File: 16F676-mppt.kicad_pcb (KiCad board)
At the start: 2 copper layers, 96.5 x 87.6 mm, 54 parts, among them J1 S+, J2 S-, J3 VB+, J4 VB-, Q1 BUK9511-55A127, Q2 BUK9511-55A127, Q3 2N2222A, Q4 2N2222A, Q5 2N2907A, Q6 2N2222A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

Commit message: Fix Bootstrap problem.
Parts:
- C2: value 10uF 50v -> 4.7uF 50v
- R1: value 2.2k -> 10k
- R15: value 2.2k -> 3.3k
- R2, R4: value 100k -> 47k
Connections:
- C2 pad 1: Net-(C2-Pad1) -> /BootStrap
- C3 pad 1: /BootStrap -> Net-(C3-Pad1)
- C4 pad 1: /BootStrap -> Net-(C3-Pad1)
- D3 pad 1: Net-(C2-Pad1) -> /BootStrap
- D3 pad 2: /BootStrap -> Net-(C7-Pad1)
- Q4 pad 3: Net-(C2-Pad1) -> /BootStrap
- R11 pad 1: /BootStrap -> Net-(C3-Pad1)
- R14 pad 1: /BootStrap -> Net-(C3-Pad1)
- R16 pad 2: /BootStrap -> Net-(C3-Pad1)
- R9 pad 1: Net-(C2-Pad1) -> /BootStrap
- U1 pad 3: /BootStrap -> Net-(C3-Pad1)
- U2 pad 8: /BootStrap -> Net-(C3-Pad1)
- U3 pad 1: /BootStrap -> Net-(C3-Pad1)
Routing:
- net Net-(C3-Pad1): track 0.00 -> 101.4 mm
- net /BootStrap: track 113.1 -> 44.7 mm
- net Net-(C2-Pad1): track 44.7 -> 0.00 mm
- net Net-(C7-Pad1): track 67.4 -> 81.8 mm

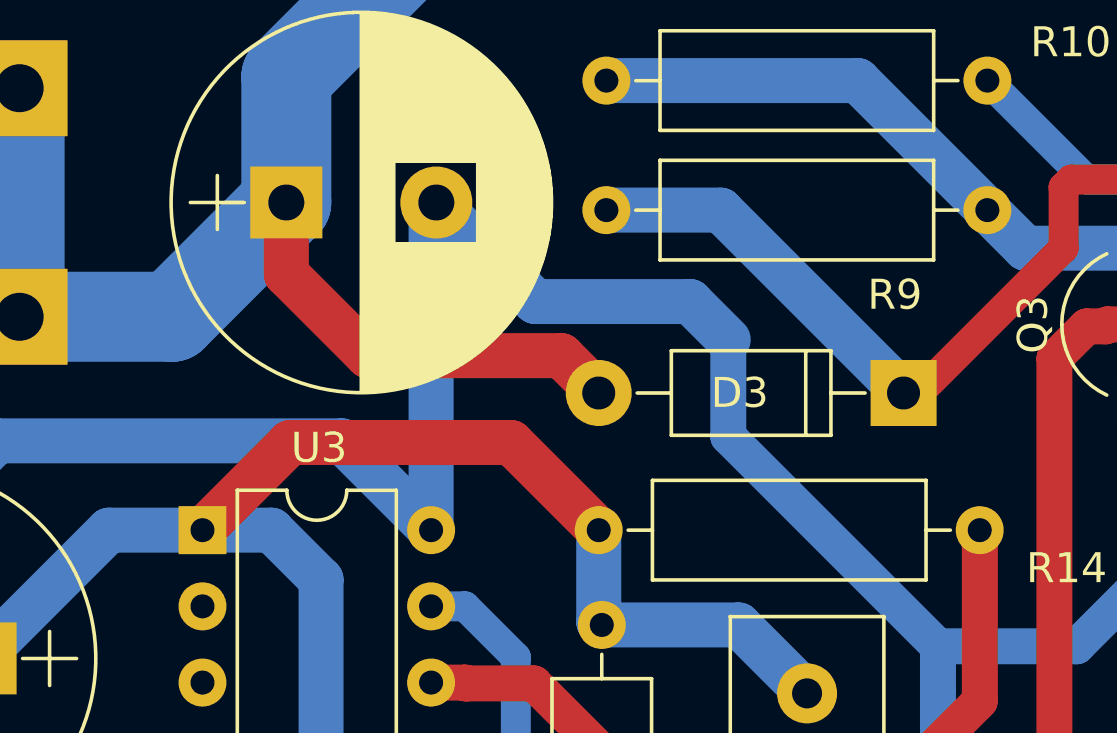
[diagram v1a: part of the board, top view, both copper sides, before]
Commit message: Revert and change diode.
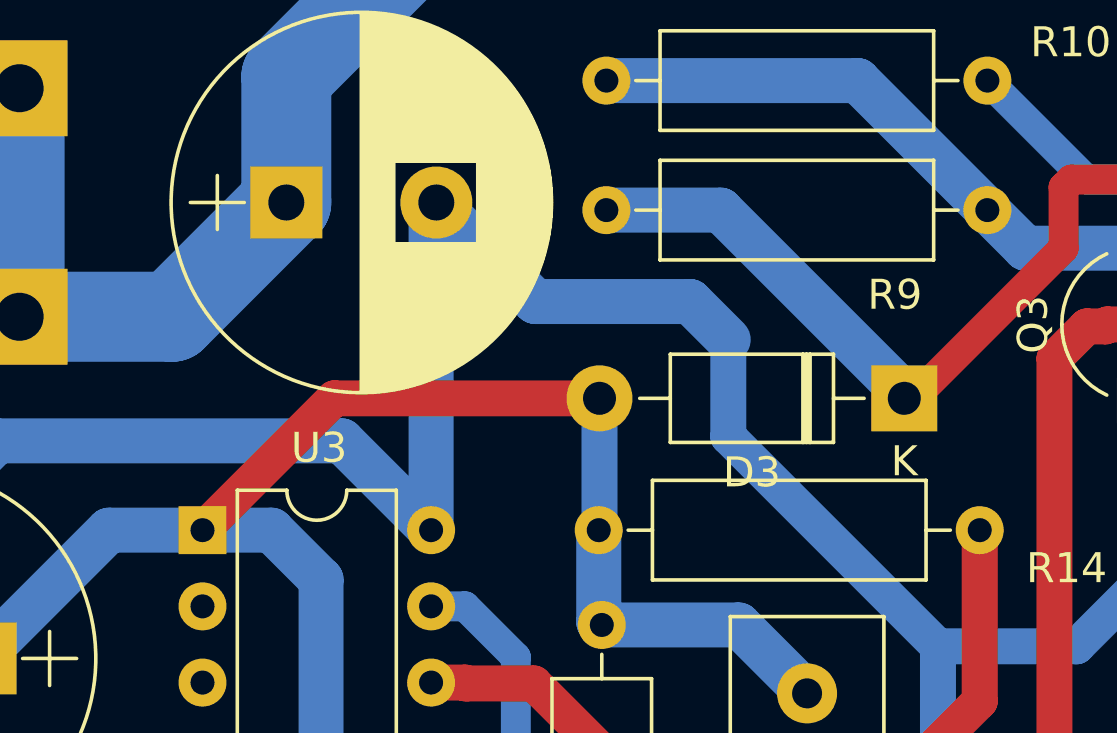
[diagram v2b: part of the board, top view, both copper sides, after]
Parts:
- D3: value 1N4148 -> 1N5819; footprint Diodes_THT:D_DO-41_SOD81_P10.16mm_Horizontal -> Diode_THT:D_DO-41_SOD81_P10.16mm_Horizontal
- moved D3 0.18 mm to (68.4, 28.9)
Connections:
- D3 pad 2: Net-(C7-Pad1) -> Net-(C3-Pad1)
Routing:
- net Net-(C7-Pad1): track 81.8 -> 67.4 mm
- net Net-(C3-Pad1): track 101.4 -> 105.2 mm

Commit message: Update SCH and PCB files.
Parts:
- added C6: 22p, Capacitor_THT:C_Rect_L4.6mm_W2.0mm_P2.50mm_MKS02_FKP02, F.Cu at (36.0, 35.8)
- added C8: 22p, Capacitor_THT:C_Rect_L4.6mm_W2.0mm_P2.50mm_MKS02_FKP02, F.Cu at (36.0, 39.0)
- added D12: BZX79C12, Diode_THT:D_DO-35_SOD27_P2.54mm_Vertical_AnodeUp, F.Cu at (95.9, 18.5)
- added Y1: 12MHz, Crystal:Crystal_HC49-U_Vertical, F.Cu at (40.5, 39.9)
- C2, C3, C5: footprint Capacitors_THT:CP_Radial_D12.5mm_P5.00mm -> Capacitor_THT:CP_Radial_D8.0mm_P2.50mm
- D3: value 1N5819 -> 1N4148; footprint Diode_THT:D_DO-41_SOD81_P10.16mm_Horizontal -> Diode_THT:D_DO-35_SOD27_P7.62mm_Horizontal
- R1: value 10k -> 1k
- R2, R4: value 47k -> 100k
- moved R11 18.6 mm to (70.8, 50.2), turned to 180 degrees
- moved D9 15.7 mm to (66.0, 71.5), turned to 90 degrees
- moved R14 15.1 mm to (70.9, 41.5), turned to 180 degrees
- moved C5 14.1 mm to (61.5, 56.5), turned to 0 degrees
- moved D8 10.7 mm to (66.0, 66.0), turned to 90 degrees
- moved R7 8.43 mm to (70.8, 46.0)
- moved C3 7.21 mm to (30.5, 39.0), turned to 90 degrees
- moved J2 4.70 mm to (15.7, 39.5)
- moved C2 3.35 mm to (84.3, 34.5)
- moved D3 2.35 mm to (66.0, 29.0)
- moved C4 2.31 mm to (65.8, 36.5), turned to 180 degrees
- moved R5 0.67 mm to (20.0, 31.1)
- moved R12 0.57 mm to (20.0, 47.5)
- moved R16 0.57 mm to (20.0, 76.5)
- moved D5 0.54 mm to (24.0, 42.1)
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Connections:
- net /PV-Current renamed /< 3.6V
- U3 pad 10: Net-(U3-Pad10) -> unconnected-(U3-RC0/AN4-Pad10)
- U3 pad 4: Net-(U3-Pad4) -> unconnected-(U3-RA3/MCLR/VPP-Pad4)
- U3 pad 5: Net-(U3-Pad5) -> unconnected-(U3-RC5-Pad5)
- U3 pad 8: Net-(U3-Pad8) -> unconnected-(U3-RC2/AN6-Pad8)
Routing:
- net GND: track 339.9 -> 296.1 mm
- net Net-(D3-A): track 105.2 -> 135.7 mm
- net /< 3.6V: track 100.8 -> 82.6 mm
- net /3.6v: track 94.4 -> 77.4 mm
- net Net-(U3-RA5/T1CKI/OSC1/CLKIN): track 0.00 -> 10.0 mm
- net Net-(U3-RA4/T1G/OSC2/AN3/CLKOUT): track 0.00 -> 10.0 mm
- net Net-(D12-K): track 11.3 -> 21.3 mm
- net -BATT: track 97.2 -> 106.6 mm
- net Net-(U3-RC1/AN5): track 17.6 -> 9.76 mm
- net Net-(Q3-B): track 31.4 -> 25.1 mm
- net Net-(D8-K): track 9.10 -> 3.00 mm
- net Net-(D1-A): track 39.1 -> 44.7 mm
- net VDD: track 26.8 -> 21.4 mm
- net Net-(D1-K): track 71.0 -> 68.8 mm
- net Net-(U3-RC3/AN7): track 58.4 -> 59.4 mm
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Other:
- net class Default removed
- net class pline removed
